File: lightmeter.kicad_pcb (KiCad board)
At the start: 2 copper layers, 34 parts, among them J1 5V input, J2 programmer, J4 VEML7700, J5 BoostConverterInput, J6 OLED Display, SW1 Shutter, SW2 Value Rot, SW3 BOOT, SW4 Setting Rot, U1 NCP1117-3.3_SOT223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

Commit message: Fixed the solanoid control part of the schematic as well as the connector for the VEML7700 light sensor, now I am really ready to start the layout proccess
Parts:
- removed J5: BoostConverterInput, Connector_JST:JST_EH_B2B-EH-A_1x02_P2.50mm_Vertical
- added D1: TS4148, Diode_SMD:D_0805_2012Metric, F.Cu at (69.3, 113.0)
- added J7: Solanoid, Connector_JST:JST_EH_B2B-EH-A_1x02_P2.50mm_Vertical, F.Cu at (65.6, 108.3)
- added Q1: FDV305N, Package_TO_SOT_SMD:SOT-23, F.Cu at (64.6, 113.7)
- added R14: 1.1K, Resistor_SMD:R_0805_2012Metric, F.Cu at (50.1, 107.1)
- added R15: 22K, Resistor_SMD:R_0805_2012Metric, F.Cu at (50.1, 110.1)
- added R16: 10k, Resistor_SMD:R_0805_2012Metric, F.Cu at (50.1, 113.0)
- added U3: FZT849, Package_TO_SOT_SMD:SOT-223-3_TabPin2, F.Cu at (57.2, 109.8)
- added U4: ~, Boost_Converter_Module_Footprint:Boost_Converter_Module, F.Cu at (50.4, 92.1)
- J4: footprint Connector_JST:JST_EH_B5B-EH-A_1x05_P2.50mm_Vertical -> Connector_PinHeader_2.54mm:PinHeader_1x05_P2.54mm_Vertical
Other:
- board outline added: 22 x 15.2 mm

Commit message: Fixed a few wrong footprints
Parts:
- SW1: footprint Button_Switch_THT:SW_PUSH-12mm -> Vertical_Push_Button:Vertical_Push_Button
- SW3: footprint Button_Switch_THT:SW_PUSH-12mm -> Button_Switch_THT:SW_PUSH_1P1T_6x3.5mm_H4.3_APEM_MJTP1243
- moved J7 74.9 mm to (124.3, 154.8)
- moved R14 74.9 mm to (108.7, 153.7)
- moved R16 74.9 mm to (108.7, 159.6)
- moved U3 74.9 mm to (115.8, 156.4)
- moved Q1 74.9 mm to (123.2, 160.2)
- moved R15 74.9 mm to (108.7, 156.6)
- moved U4 74.9 mm to (109.0, 138.7)
- moved D1 74.9 mm to (127.9, 159.5)
- moved J4 24.6 mm to (173.6, 118.8)
- moved SW3 0.79 mm to (150.2, 96.7)
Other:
- board size 22 x 15.2 mm -> 65 x 47.8 mm

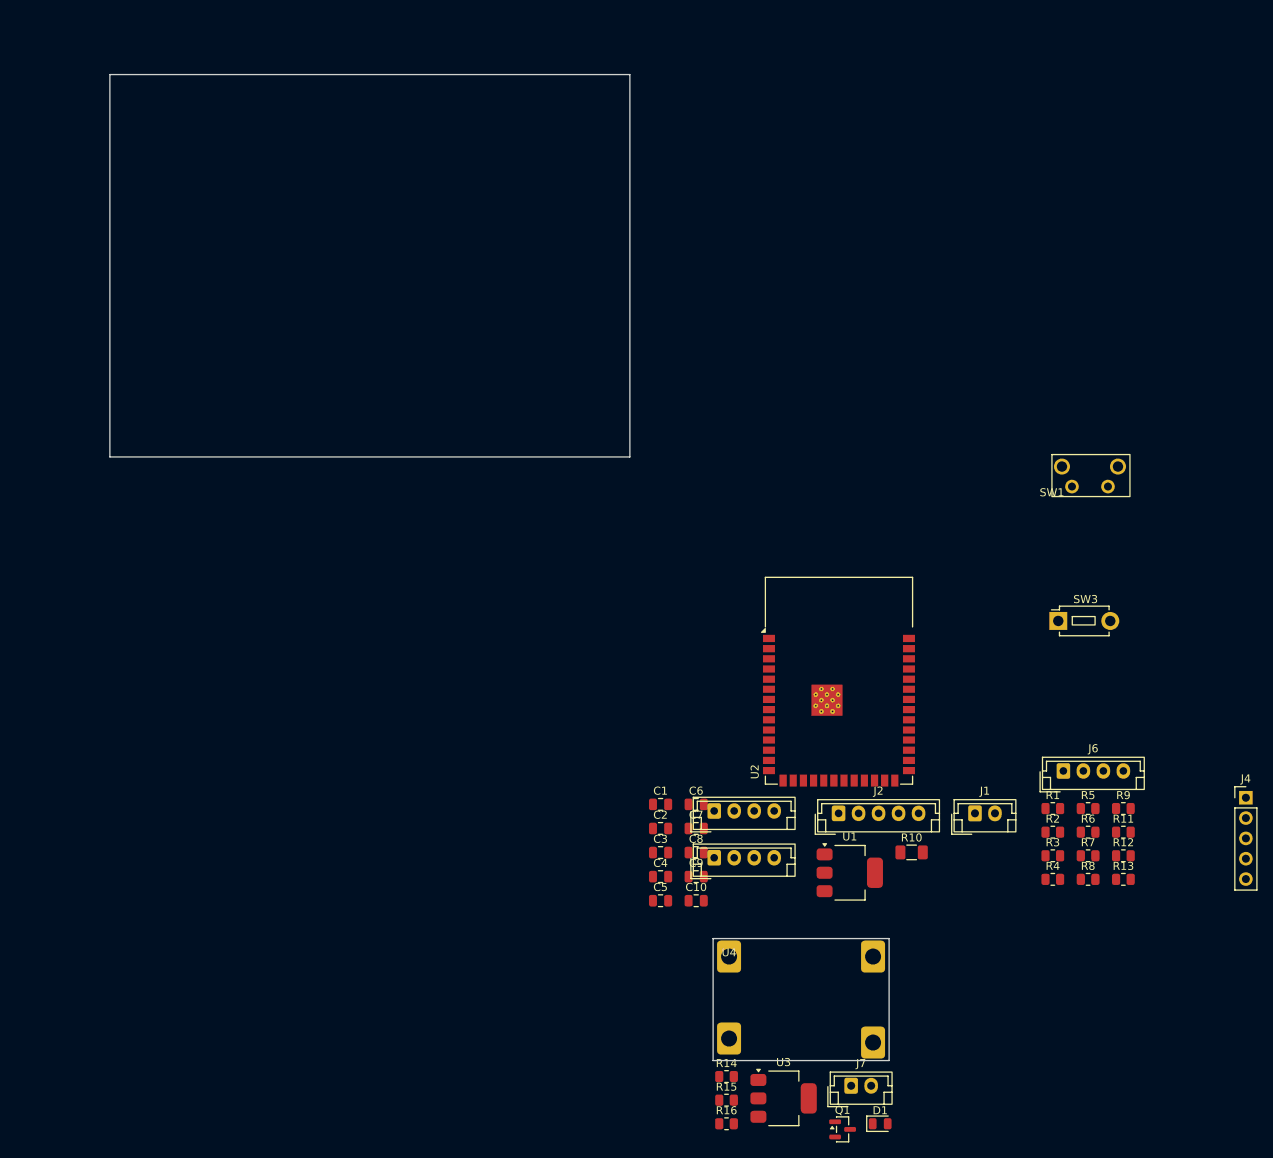
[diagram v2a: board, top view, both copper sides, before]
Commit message: ixed even more issues with the footprints, configured placement and ran autorouter. Still have settings to adjust though.
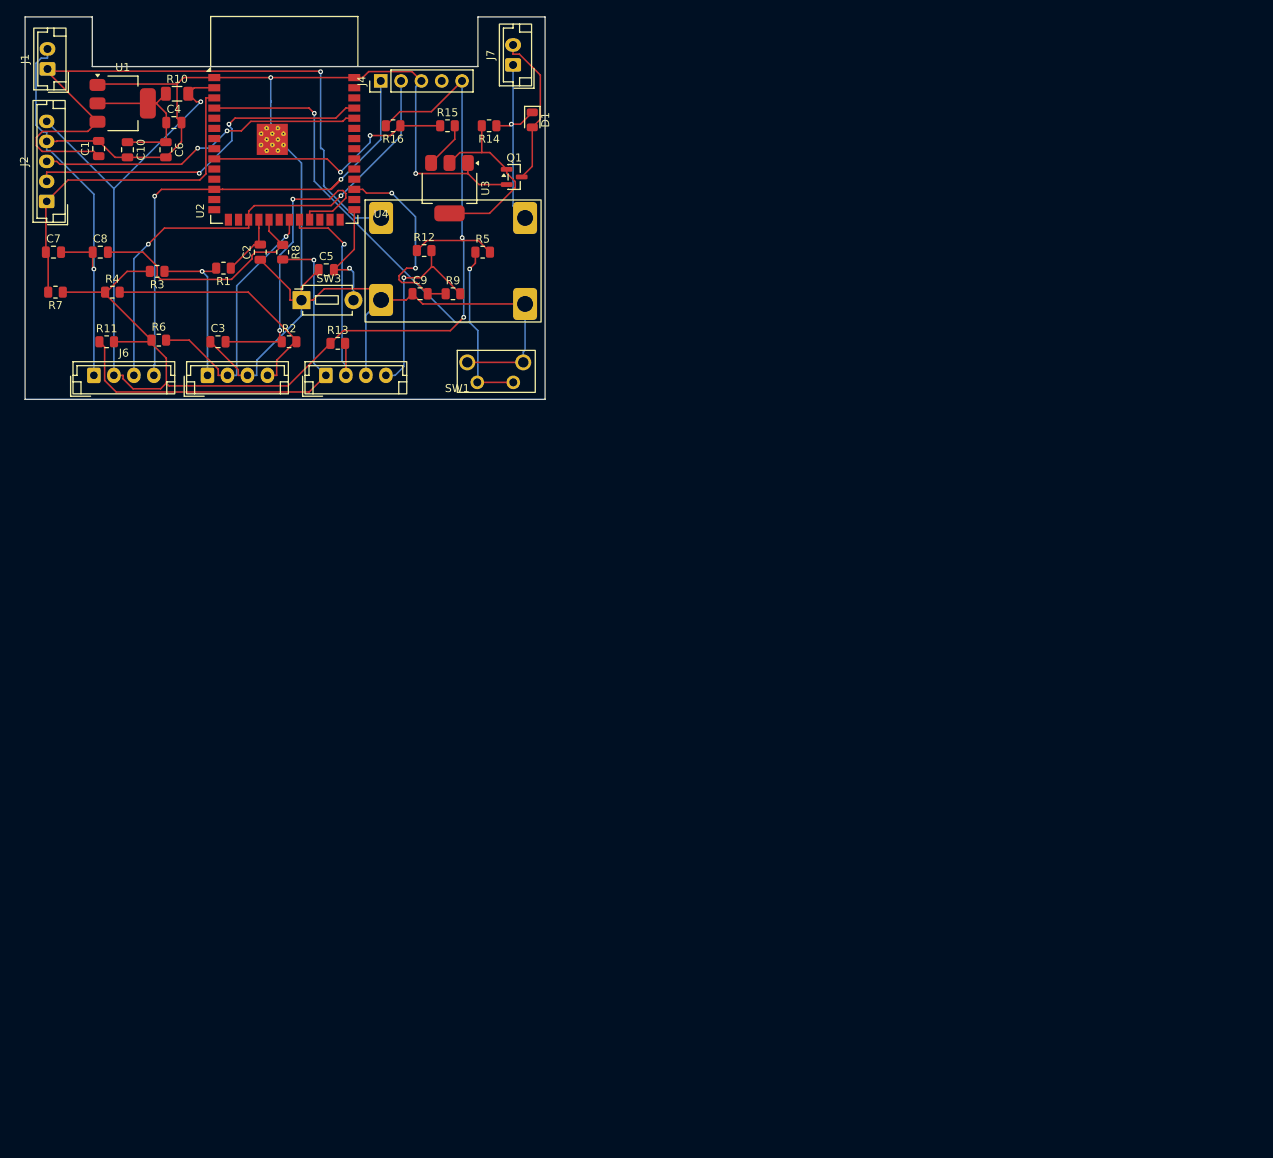
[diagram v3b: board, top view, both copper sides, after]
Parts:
- moved J1 148.7 mm to (23.8, 27.7), turned to 90 degrees
- moved R7 147.1 mm to (24.8, 55.6), turned to 180 degrees
- moved R11 141.1 mm to (31.2, 61.8)
- moved J4 140.4 mm to (65.5, 29.2), turned to 90 degrees
- moved R4 138.6 mm to (31.9, 55.6)
- moved J7 134.4 mm to (82.0, 27.2), turned to 90 degrees
- moved R3 133.7 mm to (37.5, 53.0), turned to 180 degrees
- moved D1 132.8 mm to (84.4, 34.1), turned to -90 degrees
- moved U1 132.3 mm to (33.2, 32.0)
- moved R10 132.0 mm to (40.0, 30.8)
- moved R16 131.5 mm to (67.0, 34.8), turned to 180 degrees
- moved R6 131.4 mm to (37.7, 61.6)
- moved J6 130.9 mm to (29.6, 66.0)
- moved R8 127.6 mm to (53.2, 50.6), turned to -90 degrees
- moved R15 126.7 mm to (73.8, 34.8)
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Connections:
- C10 pad 1: GND -> VCC_3V3
- C4 pad 1: GND -> VCC_3V3
- C6 pad 1: GND -> VCC_3V3
- R10 pad 1: GND -> VCC_3V3
- U1 pad 2: GND -> VCC_3V3
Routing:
- net GND: track 0.00 -> 273.1 mm, vias 0 -> 3
- net ESP_3V3: track 0.00 -> 188.0 mm, vias 0 -> 3
- net +5V: track 0.00 -> 84.7 mm, vias 0 -> 1
- net /GPIO4: track 0.00 -> 69.5 mm, vias 0 -> 2
- net /GPIO8: track 0.00 -> 64.5 mm, vias 0 -> 2
- net /GPIO9: track 0.00 -> 62.4 mm, vias 0 -> 2
- net Net-(R11-Pad1): track 0.00 -> 53.2 mm, vias 0 -> 1
- net /U0TXD: track 0.00 -> 44.8 mm, vias 0 -> 2
- net /CHIP_PU: track 0.00 -> 43.4 mm
- net /U0RXD: track 0.00 -> 41.0 mm, vias 0 -> 2
- net /GPIO21: track 0.00 -> 39.6 mm, vias 0 -> 2
- net /GPIO13: track 0.00 -> 33.3 mm, vias 0 -> 1
- net /GPIO16: track 0.00 -> 31.8 mm, vias 0 -> 2
- net Net-(R2-Pad2): track 0.00 -> 31.2 mm
- net /GPIO11: track 0.00 -> 29.9 mm
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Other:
- outline, holes or cut-outs redrawn

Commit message: Finished PCB. I will review it one more time and send it for fabrication.
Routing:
- net GND: track 273.1 -> 1.22 mm, vias 3 -> 14
- net /GPIO9: track 62.4 -> 101.3 mm
- net +5V: track 84.7 -> 54.0 mm
- net /GPIO21: track 39.6 -> 26.4 mm
- net /GPIO13: track 33.3 -> 41.5 mm, vias 1 -> 2
- net /GPIO8: track 64.5 -> 57.0 mm
- net ESP_3V3: track 188.0 -> 182.9 mm
- net Net-(Q1-G): track 24.2 -> 19.8 mm
- net /GPIO36: track 25.0 -> 21.3 mm, vias 2 -> 0
- net /GPIO14: track 28.2 -> 31.8 mm
- net Net-(R12-Pad2): track 24.9 -> 21.8 mm, vias 1 -> 0
- net /CHIP_PU: track 43.4 -> 40.5 mm
- net Net-(R11-Pad1): track 53.2 -> 55.8 mm
- net /U0TXD: track 44.8 -> 47.3 mm, vias 2 -> 3
- net /GPIO16: track 31.8 -> 30.1 mm
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- added copper zone on B.Cu, net GND
- added copper zone on F.Cu, net GND
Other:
- outline, holes or cut-outs redrawn
